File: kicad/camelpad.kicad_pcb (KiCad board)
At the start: 2 copper layers, 90 x 75 mm, 29 parts, among them J1 USB_C_Receptacle_USB2.0_16P, J2 USB_C_Receptacle_USB2.0_16P, J3 AVR-UPDI, SW1 SWITCH_PUSHBUTTON_KAILH_SOCKET, SW2 SWITCH_PUSHBUTTON_KAILH_SOCKET, SW3 SWITCH_PUSHBUTTON_KAILH_SOCKET, SW4 SWITCH_PUSHBUTTON_KAILH_SOCKET, SW5 SWITCH_PUSHBUTTON_KAILH_SOCKET, SW6 SWITCH_PUSHBUTTON_KAILH_SOCKET, U1 ATtiny816-M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

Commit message: Schematic Cleanup
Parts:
- removed CONN1: ~, camelpad:JST_SH_BM04B-SRSS-TB_1x04-1MP_P1.00mm_Vertical
- removed J3: AVR-UPDI, camelpad:JST_SH_BM03B-SRSS-TB_1x03-1MP_P1.00mm_Vertical
- added I2C1: I2C, camelpad:JST_SH_BM04B-SRSS-TB_1x04-1MP_P1.00mm_Vertical, F.Cu at (131.4, 31.2)
- added R1: 3K3, camelpad:R_0402_1005Metric, F.Cu at (111.3, 30.2)
- added UPDI1: AVR-UPDI, camelpad:JST_SH_BM04B-SRSS-TB_1x04-1MP_P1.00mm_Vertical, F.Cu at (107.7, 31.2)
- moved C1 12.6 mm to (124.9, 29.8)
- moved D7 12.6 mm to (119.4, 31.8)
- moved RN1 12.6 mm to (124.0, 34.4)
- moved U2 12.6 mm to (119.4, 29.0)
- moved C3 12.4 mm to (113.5, 29.0)
- moved C2 12.4 mm to (115.6, 29.0)
- moved J2 0.58 mm to (75.1, 38.6)
- moved J1 0.57 mm to (75.0, 29.4)
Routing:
- net VIN: track 20.2 -> 44.1 mm
- net /SCL: track 19.8 -> 25.9 mm
- net /SDA: track 21.1 -> 27.1 mm
- net Net-(UPDI1-TX): track 0.00 -> 2.29 mm
- net GND: track 69.9 -> 68.2 mm
- net /SW1: track 26.1 -> 27.5 mm
- net /UPDI: track 17.7 -> 18.7 mm, vias 0 -> 2
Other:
- board text added: "JLCJLCJLCJLCJLCJLCJLC"

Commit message: Update KiCad project
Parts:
- D1, D2, D3, D4, D5, D6: footprint Diode_SMD:D_SOD-323 -> camelpad:D_SOD-323
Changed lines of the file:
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@@
 			)
 		)
-		(property "Datasheet" ""
+		(property "Datasheet" "~"
 			(at 0 0 0)
 			(layer "F.Fab")
@@
 			)
 		)
-		(property "Description" ""
+		(property "Description" "Push button switch, generic, two pins"
 			(at 0 0 0)
 			(layer "F.Fab")
@@
 		(sheetname "/")
 		(sheetfile "camelpad.kicad_sch")
+		(attr exclude_from_bom)
 		(fp_line
 			(start -9.525 8.255)
@@
 		)
 	)
-	(footprint "Diode_SMD:D_SOD-323"
+	(footprint "camelpad:D_SOD-323"
 		(layer "F.Cu")
 		(at 109.75 95.9825 180)
@@
 		(tags "SOD-323")
 		(property "Reference" "D6"
-			(at 0 -1.85 0)
+			(at 0 -1.85 180)
 			(layer "F.SilkS")
+			(hide yes)
 			(effects
 				(font
@@
 		)
 		(property "Value" "1N4148"
-			(at 0.1 1.9 0)
-			(layer "F.Fab")
+			(at 0 -1.8175 180)
+			(layer "F.SilkS")
 			(effects
 				(font
 					(size 1 1)
 					(thickness 0.15)
+					(italic yes)
 				)
 			)
 		)
-		(property "Datasheet" "https://www.vishay.com/docs/85751/1n4148ws.pdf"
+		(property "Datasheet" "https://assets.nexperia.com/documents/data-sheet/1N4148_1N4448.pdf"
 			(at 0 0 180)
 			(unlocked yes)
@@
 			)
 		)
-		(property "Description" "75V 0.15A Fast switching Diode, SOD-323"
+		(property "Description" "100V 0.15A standard switching diode, DO-35"
 			(at 0 0 180)
 			(unlocked yes)
@@
 			)
 		)
-		(property ki_fp_filters "D*SOD?323*")
+		(property ki_fp_filters "D*DO?35*")
 		(sheetname "/")
 		(sheetfile "camelpad.kicad_sch")
@@
 		)
 		(fp_text user "${REFERENCE}"
-			(at 0 -1.85 0)
+			(at 0 -1.85 180)
 			(layer "F.Fab")
 			(effects
@@
 			)
 		)
-		(property "Datasheet" ""
+		(property "Datasheet" "~"
 			(at 0 0 0)
 			(layer "F.Fab")
@@
 			)
 		)
-		(property "Description" ""
+		(property "Description" "Push button switch, generic, two pins"
 			(at 0 0 0)
 			(layer "F.Fab")
@@
 		(sheetname "/")
 		(sheetfile "camelpad.kicad_sch")
+		(attr exclude_from_bom)
 		(fp_line
 			(start -9.525 8.255)
@@
 		)
 	)
-	(footprint "Diode_SMD:D_SOD-323"
+	(footprint "camelpad:D_SOD-323"
 		(layer "F.Cu")
 		(at 100.31 68.25 180)
@@
 		(tags "SOD-323")
 		(property "Reference" "D2"
-			(at 0 -1.85 0)
+			(at 0 -1.85 180)
 			(layer "F.SilkS")
+			(hide yes)
 			(effects
 				(font
@@
 		)
 		(property "Value" "1N4148"
-			(at 0.1 1.9 0)
+			(at 0 -2.05 180)
 			(layer "F.SilkS")
 			(effects
@@
 					(size 1 1)
 					(thickness 0.15)
+					(italic yes)
 				)
 			)
 		)
-		(property "Datasheet" "https://www.vishay.com/docs/85751/1n4148ws.pdf"
+		(property "Datasheet" "https://assets.nexperia.com/documents/data-sheet/1N4148_1N4448.pdf"
 			(at 0 0 180)
 			(unlocked yes)
@@
 			)
 		)
-		(property "Description" "75V 0.15A Fast switching Diode, SOD-323"
+		(property "Description" "100V 0.15A standard switching diode, DO-35"
 			(at 0 0 180)
 			(unlocked yes)
@@
 			)
 		)
-		(property ki_fp_filters "D*SOD?323*")
+		(property ki_fp_filters "D*DO?35*")
 		(sheetname "/")
 		(sheetfile "camelpad.kicad_sch")
@@
 		)
 		(fp_text user "${REFERENCE}"
-			(at 0 -1.85 0)
+			(at 0 -1.85 180)
 			(layer "F.Fab")
 			(effects
@@
 			)
 		)
-		(property "Datasheet" ""
+		(property "Datasheet" "~"
 			(at 0 0 0)
 			(layer "F.Fab")
@@
 			)
 		)
-		(property "Description" ""
+		(property "Description" "Push button switch, generic, two pins"
 			(at 0 0 0)
 			(layer "F.Fab")
@@
 		(sheetname "/")
 		(sheetfile "camelpad.kicad_sch")
+		(attr exclude_from_bom)
 		(fp_line
 			(start -9.525 8.255)
@@
 		(embedded_fonts no)
 	)
-	(footprint "Diode_SMD:D_SOD-323"
+	(footprint "camelpad:D_SOD-323"
 		(layer "F.Cu")
 		(at 69 95.9825 180)
@@
 		(tags "SOD-323")
 		(property "Reference" "D5"
-			(at 0 -1.85 0)
+			(at 0 -1.85 180)
 			(layer "F.SilkS")
+			(hide yes)
 			(effects
 				(font
@@
 		)
 		(property "Value" "1N4148"
-			(at 0.1 1.9 0)
-			(layer "F.Fab")
+			(at 0 -1.8175 180)
+			(layer "F.SilkS")
 			(effects
 				(font
 					(size 1 1)
 					(thickness 0.15)
+					(italic yes)
 				)
 			)
 		)
-		(property "Datasheet" "https://www.vishay.com/docs/85751/1n4148ws.pdf"
+		(property "Datasheet" "https://assets.nexperia.com/documents/data-sheet/1N4148_1N4448.pdf"
 			(at 0 0 180)
 			(unlocked yes)
@@
 			)
 		)
-		(property "Description" "75V 0.15A Fast switching Diode, SOD-323"
+		(property "Description" "100V 0.15A standard switching diode, DO-35"
 			(at 0 0 180)
 			(unlocked yes)
@@
 			)
 		)
-		(property ki_fp_filters "D*SOD?323*")
+		(property ki_fp_filters "D*DO?35*")
 		(sheetname "/")
 		(sheetfile "camelpad.kicad_sch")
@@
 		)
 		(fp_text user "${REFERENCE}"
-			(at 0 -1.85 0)
+			(at 0 -1.85 180)
 			(layer "F.Fab")
 			(effects
@@
 		)
 	)
-	(footprint "Diode_SMD:D_SOD-323"
+	(footprint "camelpad:D_SOD-323"
 		(layer "F.Cu")
 		(at 79.27 68.2325 180)
@@
 		(tags "SOD-323")
 		(property "Reference" "D3"
-			(at 0 -1.85 0)
+			(at 0 -1.85 180)
 			(layer "F.SilkS")
+			(hide yes)
 			(effects
 				(font
@@
 		)
 		(property "Value" "1N4148"
-			(at 0.1 1.9 0)
+			(at 0 -1.8675 180)
 			(layer "F.SilkS")
 			(effects
@@
 					(size 1 1)
 					(thickness 0.15)
+					(italic yes)
 				)
 			)
 		)
-		(property "Datasheet" "https://www.vishay.com/docs/85751/1n4148ws.pdf"
+		(property "Datasheet" "https://assets.nexperia.com/documents/data-sheet/1N4148_1N4448.pdf"
 			(at 0 0 180)
 			(unlocked yes)
@@
 			)
 		)
-		(property "Description" "75V 0.15A Fast switching Diode, SOD-323"
+		(property "Description" "100V 0.15A standard switching diode, DO-35"
 			(at 0 0 180)
 			(unlocked yes)
@@
 			)
 		)
-		(property ki_fp_filters "D*SOD?323*")
+		(property ki_fp_filters "D*DO?35*")
 		(sheetname "/")
 		(sheetfile "camelpad.kicad_sch")
@@
 		)
 		(fp_text user "${REFERENCE}"
-			(at 0 -1.85 0)
+			(at 0 -1.85 180)
 			(layer "F.Fab")
 			(effects
@@
 		)
 	)
-	(footprint "Diode_SMD:D_SOD-323"
+	(footprint "camelpad:D_SOD-323"
 		(layer "F.Cu")
 		(at 58.25 68.2325 180)
@@
 		(tags "SOD-323")
 		(property "Reference" "D4"
-			(at 0 -1.85 0)
+			(at 0 -1.85 180)
 			(layer "F.SilkS")
+			(hide yes)
 			(effects
 				(font
@@
 		)
 		(property "Value" "1N4148"
-			(at 0.1 1.9 0)
-			(layer "F.Fab")
+			(at 0.05 -1.9675 180)
+			(layer "F.SilkS")
 			(effects
 				(font
 					(size 1 1)
 					(thickness 0.15)
+					(italic yes)
 				)
 			)
 		)
-		(property "Datasheet" "https://www.vishay.com/docs/85751/1n4148ws.pdf"
+		(property "Datasheet" "https://assets.nexperia.com/documents/data-sheet/1N4148_1N4448.pdf"
 			(at 0 0 180)
 			(unlocked yes)
@@
 			)
 		)
-		(property "Description" "75V 0.15A Fast switching Diode, SOD-323"
+		(property "Description" "100V 0.15A standard switching diode, DO-35"
 			(at 0 0 180)
 			(unlocked yes)
@@
 			)
 		)
-		(property ki_fp_filters "D*SOD?323*")
+		(property ki_fp_filters "D*DO?35*")
 		(sheetname "/")
 		(sheetfile "camelpad.kicad_sch")
@@
 		)
 		(fp_text user "${REFERENCE}"
-			(at 0 -1.85 0)
+			(at 0 -1.85 180)
 			(layer "F.Fab")
 			(effects
@@
 			)
 		)
-		(property "Datasheet" ""
+		(property "Datasheet" "~"
 			(at 0 0 0)
 			(layer "F.Fab")
@@
 			)
 		)
-		(property "Description" ""
+		(property "Description" "Push button switch, generic, two pins"
 			(at 0 0 0)
 			(layer "F.Fab")
@@
 		(sheetname "/")
 		(sheetfile "camelpad.kicad_sch")
+		(attr exclude_from_bom)
 		(fp_line
 			(start -9.525 8.255)
@@
 			)
 		)
-		(property "Datasheet" ""
+		(property "Datasheet" "~"
 			(at 0 0 0)
 			(layer "F.Fab")
@@
 			)
 		)
-		(property "Description" ""
+		(property "Description" "Push button switch, generic, two pins"
 			(at 0 0 0)
 			(layer "F.Fab")
@@
 		(sheetname "/")
 		(sheetfile "camelpad.kicad_sch")
+		(attr exclude_from_bom)
 		(fp_line
 			(start -9.525 8.255)
@@
 		(embedded_fonts no)
 	)
-	(footprint "Diode_SMD:D_SOD-323"
+	(footprint "camelpad:D_SOD-323"
 		(layer "F.Cu")
 		(at 121.25 68.2325 180)
@@
 		(tags "SOD-323")
 		(property "Reference" "D1"
-			(at 0 -1.85 0)
+			(at 0 -1.85 180)
 			(layer "F.SilkS")
 			(hide yes)
@@
 		)
 		(property "Value" "1N4148"
-			(at 0.1 1.9 0)
+			(at 0 -1.9675 180)
 			(layer "F.SilkS")
 			(effects
@@
 					(size 1 1)
 					(thickness 0.15)
+					(italic yes)
 				)
 			)
 		)
-		(property "Datasheet" "https://www.vishay.com/docs/85751/1n4148ws.pdf"
+		(property "Datasheet" "https://assets.nexperia.com/documents/data-sheet/1N4148_1N4448.pdf"
 			(at 0 0 180)
 			(unlocked yes)
@@
 			)
 		)
-		(property "Description" "75V 0.15A Fast switching Diode, SOD-323"
+		(property "Description" "100V 0.15A standard switching diode, DO-35"
 			(at 0 0 180)
 			(unlocked yes)
@@
 			)
 		)
-		(property ki_fp_filters "D*SOD?323*")
+		(property ki_fp_filters "D*DO?35*")
 		(sheetname "/")
 		(sheetfile "camelpad.kicad_sch")
@@
 		)
 		(fp_text user "${REFERENCE}"
-			(at 0 -1.85 0)
+			(at 0 -1.85 180)
 			(layer "F.Fab")
 			(effects
@@
 			)
 		)
-		(property "Datasheet" ""
+		(property "Datasheet" "~"
 			(at 0 0 0)
 			(layer "F.Fab")
@@
 			)
 		)
-		(property "Description" ""
+		(property "Description" "Push button switch, generic, two pins"
 			(at 0 0 0)
 			(layer "F.Fab")
@@
 		(sheetname "/")
 		(sheetfile "camelpad.kicad_sch")
+		(attr exclude_from_bom)
 		(fp_line
 			(start -9.525 8.255)

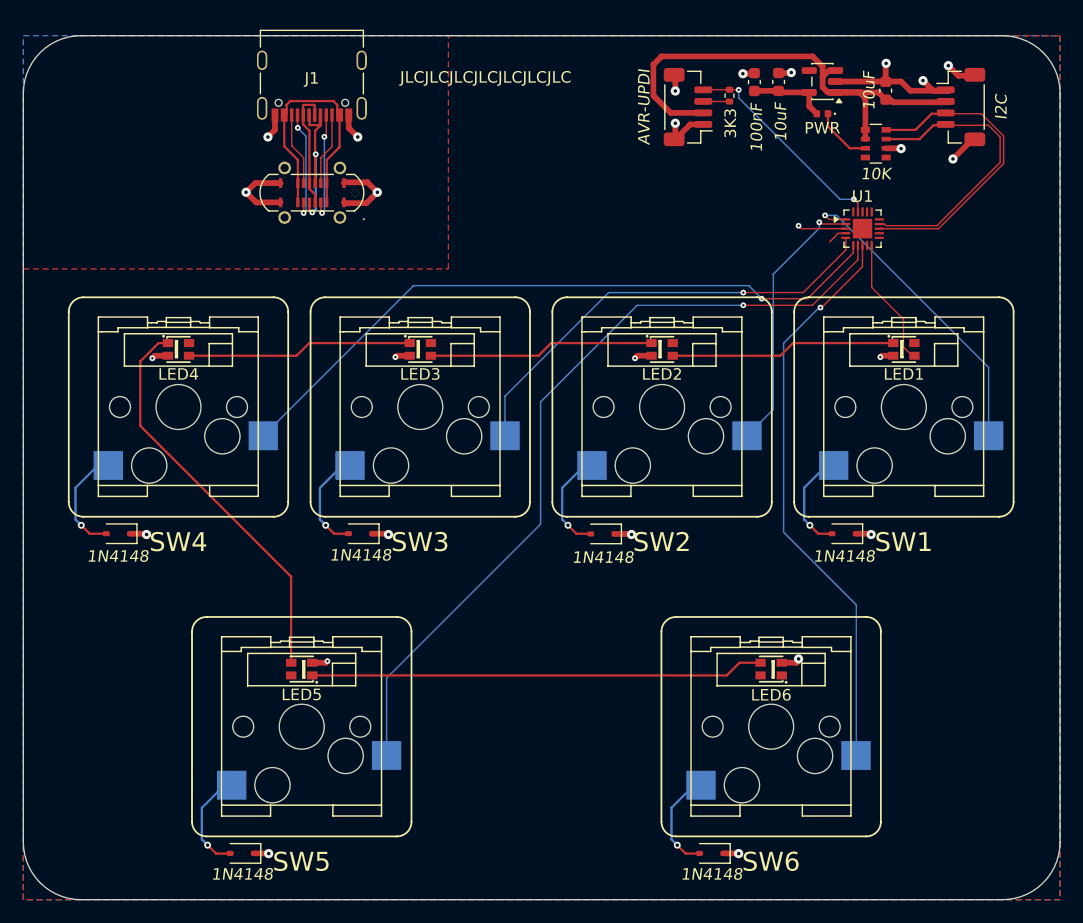
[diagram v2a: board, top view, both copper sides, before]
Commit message: Update usb connector to molex picoblade
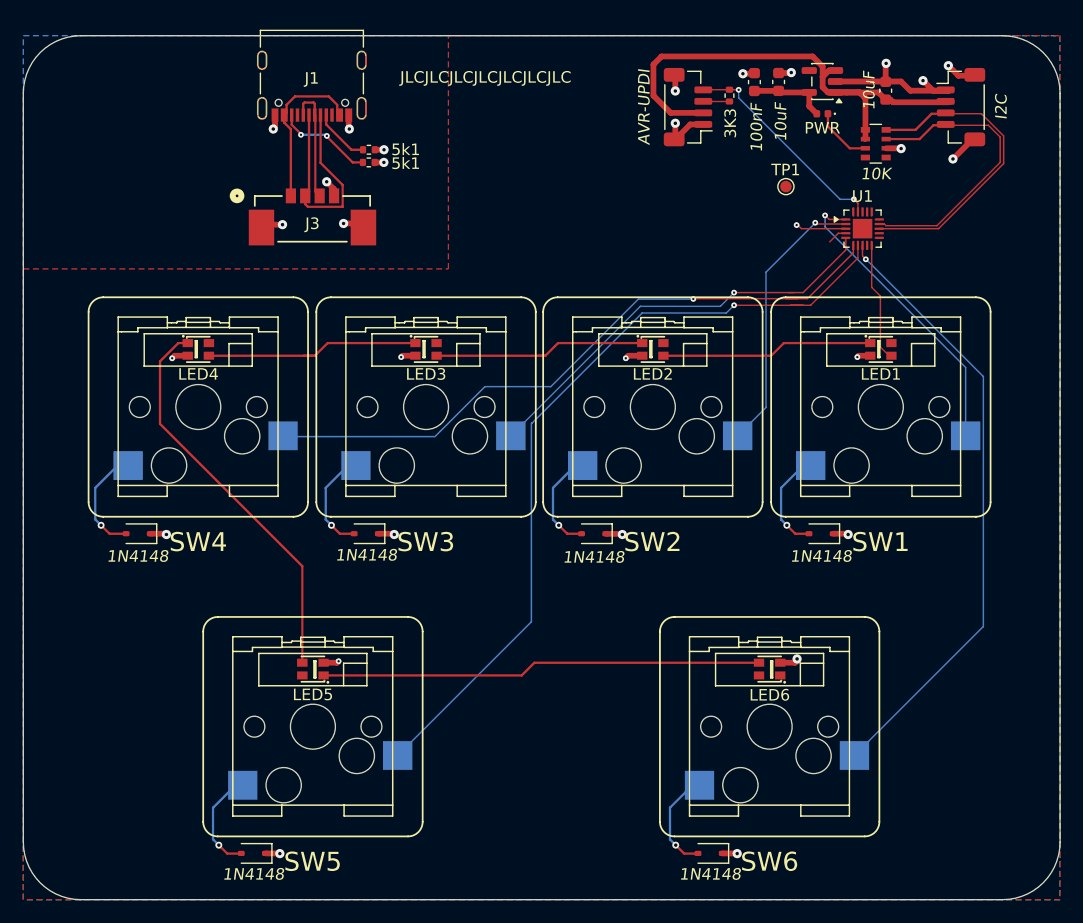
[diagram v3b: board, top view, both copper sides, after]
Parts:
- removed J2: USB_C_Receptacle_USB2.0_16P, camelpad:USB-C-SMD_GT-USB-7055E
- added J3: Molex PicoBlade 533980471, camelpad:CONN_53398_04_MOL, F.Cu at (75.1, 40.9)
- added R2: 5k1, camelpad:R_0402_1005Metric, F.Cu at (80.0, 36.0)
- added R3: 5k1, camelpad:R_0402_1005Metric, F.Cu at (80.0, 34.9)
- added TP1: TestPoint, TestPoint:TestPoint_Pad_D1.0mm, F.Cu at (116.2, 38.1)
- moved D1 2.00 mm to (119.2, 68.2)
- moved LED1 2.00 mm to (124.4, 52.2)
- moved SW1 2.00 mm to (124.4, 57.2)
- moved D4 1.72 mm to (60.0, 68.2)
- moved LED4 1.72 mm to (65.2, 52.2)
- moved SW4 1.72 mm to (65.2, 57.2)
- moved D5 0.97 mm to (70.0, 96.0)
- moved LED5 0.97 mm to (75.1, 80.0)
- moved SW5 0.97 mm to (75.1, 85.0)
- moved D2 0.80 mm to (99.5, 68.2)
- moved LED2 0.80 mm to (104.7, 52.2)
- moved SW2 0.80 mm to (104.7, 57.2)
- moved D3 0.50 mm to (79.8, 68.2)
- moved LED3 0.50 mm to (85.0, 52.2)
- moved SW3 0.50 mm to (85.0, 57.2)
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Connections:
- net Net-(J1-D+-PadA6) renamed /D+
- net Net-(J1-D--PadA7) renamed /D-
- J1 pad A8: Net-(J1-SBU1) -> unconnected-(J1-SBU1-PadA8)
- J1 pad B8: Net-(J1-SBU2) -> unconnected-(J1-SBU2-PadB8)
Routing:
- net Net-(J1-SBU1): track 9.81 -> 0.00 mm, vias 2 -> 0
- net VBUS: track 22.7 -> 14.2 mm
- net GND: track 68.2 -> 60.1 mm, vias 26 -> 29
- net Net-(J1-SBU2): track 6.31 -> 0.00 mm
- net /D-: track 15.0 -> 20.0 mm, vias 2 -> 0
- net Net-(J1-CC1): track 9.62 -> 4.93 mm, vias 2 -> 0
- net /SW6: track 49.9 -> 53.3 mm
- net Net-(J1-CC2): track 6.34 -> 8.45 mm, vias 0 -> 2
- net /SW3: track 39.3 -> 37.3 mm
- net /SW4: track 59.4 -> 57.9 mm
- net /SW1: track 27.5 -> 26.1 mm
- net Net-(LED1-DOUT): track 19.6 -> 18.4 mm
- net Net-(LED5-DOUT): track 39.4 -> 38.3 mm
- net /LED: track 11.2 -> 10.4 mm
- net Net-(LED2-DOUT): track 19.6 -> 18.8 mm

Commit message: Update design rules and component footprints in camelpad project
- Added multiple DRC exclusions for silk and copper layers in camelpad.kicad_pro to improve layout integrity.
- Adjusted solder mask to copper clearance from 0.0 to 0.005 for better manufacturing tolerance.
- Updated component footprints in camelpad.kicad_sch from 0402 to 0603 for resistors and capacitors to accommodate new specifications.
- Changed LED footprint to a specific camelpad variant for improved compatibility.
- Modified resistor array footprints from 4x0603 to 4x1206 to reflect updated design requirements.
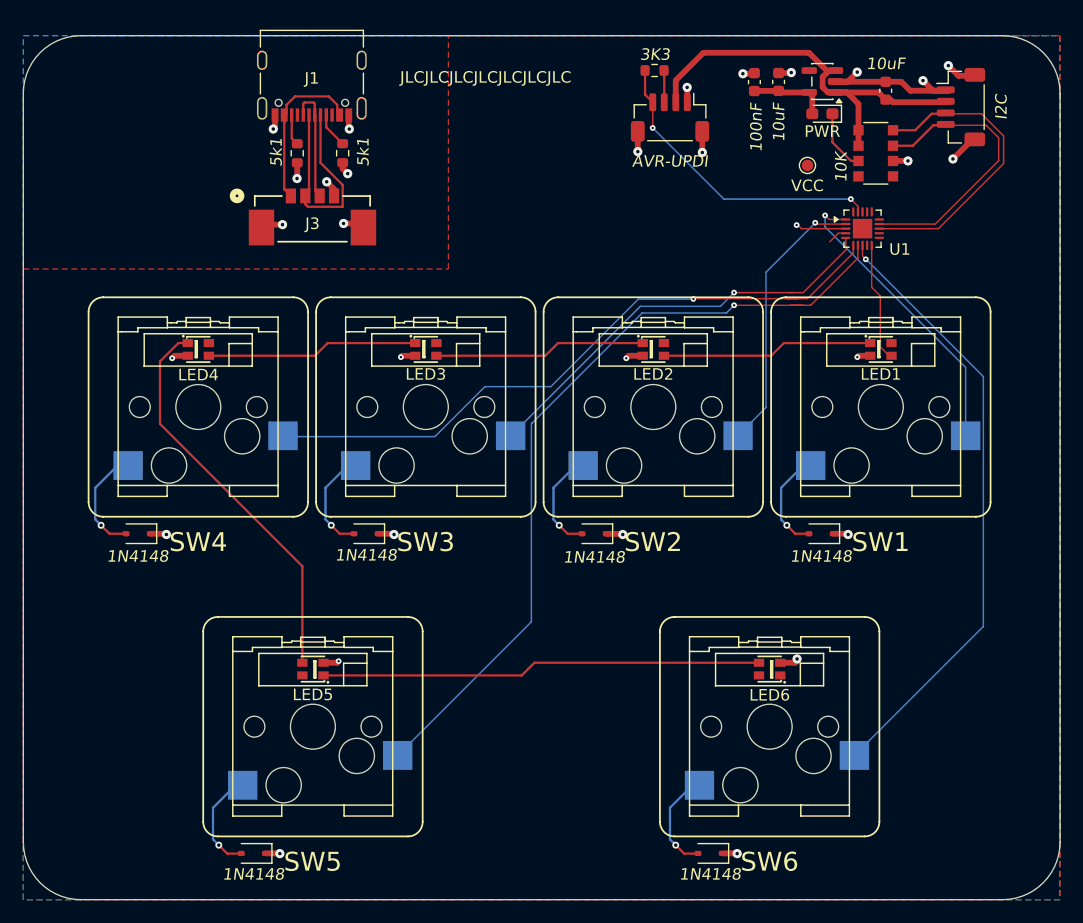
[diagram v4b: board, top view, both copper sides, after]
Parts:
- C1, C2, C3: footprint Capacitor_SMD:C_0603_1608Metric -> camelpad:C_0603_1608Metric
- D7: footprint LED_SMD:LED_0402_1005Metric -> camelpad:LED_0603_1608Metric_Pad1.05x0.95mm_HandSolder
- R1, R2, R3: footprint camelpad:R_0402_1005Metric -> camelpad:R_0603_1608Metric
- RN1: footprint camelpad:R_Array_Convex_4x0603 -> camelpad:R_Array_Convex_4x1206
- moved R1 6.86 mm to (104.8, 28.0), turned to 180 degrees
- moved R2 6.26 mm to (73.8, 35.2), turned to 90 degrees
- moved VCC 2.62 mm to (118.1, 36.3)
- moved R3 2.30 mm to (77.7, 35.2), turned to 90 degrees
- moved UPDI1 1.80 mm to (106.1, 32.1), turned to 180 degrees
- moved RN1 0.83 mm to (124.0, 35.2)
- renumbered TP1 to VCC
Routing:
- net /UPDI: track 18.7 -> 26.2 mm
- net VIN: track 44.1 -> 36.7 mm
- net Net-(J1-CC2): track 8.45 -> 2.69 mm, vias 2 -> 0
- net Net-(J1-CC1): track 4.93 -> 3.08 mm
- net Net-(LED3-DOUT): track 19.5 -> 18.5 mm
- net /SCL: track 25.9 -> 25.0 mm
- net Net-(LED2-DOUT): track 18.8 -> 18.2 mm
- net /SDA: track 27.1 -> 26.5 mm
- net GND: track 60.1 -> 60.2 mm, vias 29 -> 30
